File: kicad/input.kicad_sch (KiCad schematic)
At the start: 210 parts, among them J1 IN_1, J2 IN_2, Q1 CSD13380F3, Q5 CSD13380F3, SW1 RotaryEncoder, SW10 DG1411EEQ, SW11 DG1413EEQ, SW2 INST_IND_1, SW3 DG1413EEQ, SW4 DG1411EEQ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

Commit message: inst/line inverter
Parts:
- added C199, C200: 100nF, symbol Device:C
- added R127, R128, R129, R130: 1k, symbol Device:R_US
- added U24: OPA1612AxD, symbol Amplifier_Operational:OPA1612AxD
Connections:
- net +15V: now also C199.1, U24.8 (V+)
- net -15V: now also C200.1, U24.4 (V-)
- net GNDA: now also C199.2, C200.2, U24.3 (+), U24.6 (-); no longer SW11.3 (S1), SW5.3 (S1)
- net at R21.2, SW4.7 (D4), U5.1: now also SW5.3 (S1), R128.1; no longer SW5.6 (S4)
- net at R52.2, SW10.7 (D4): now also SW11.3 (S1), R129.1, U24.1; no longer SW11.6 (S4), U5.7
- net at R50.1, R57.2: now also U24.2 (-); no longer U5.5 (+)
- new net: R127.1, R128.2, U5.5 (+)
- new net: R127.2, SW5.6 (S4), U5.7
- new net: R130.2, SW11.6 (S4), U24.7
- new net: R129.2, R130.1, U24.5 (+)
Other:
- moved on the sheet: C187, C188, C70, Q1, R125, R126, R43, R45, R47, R48, R50, R51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

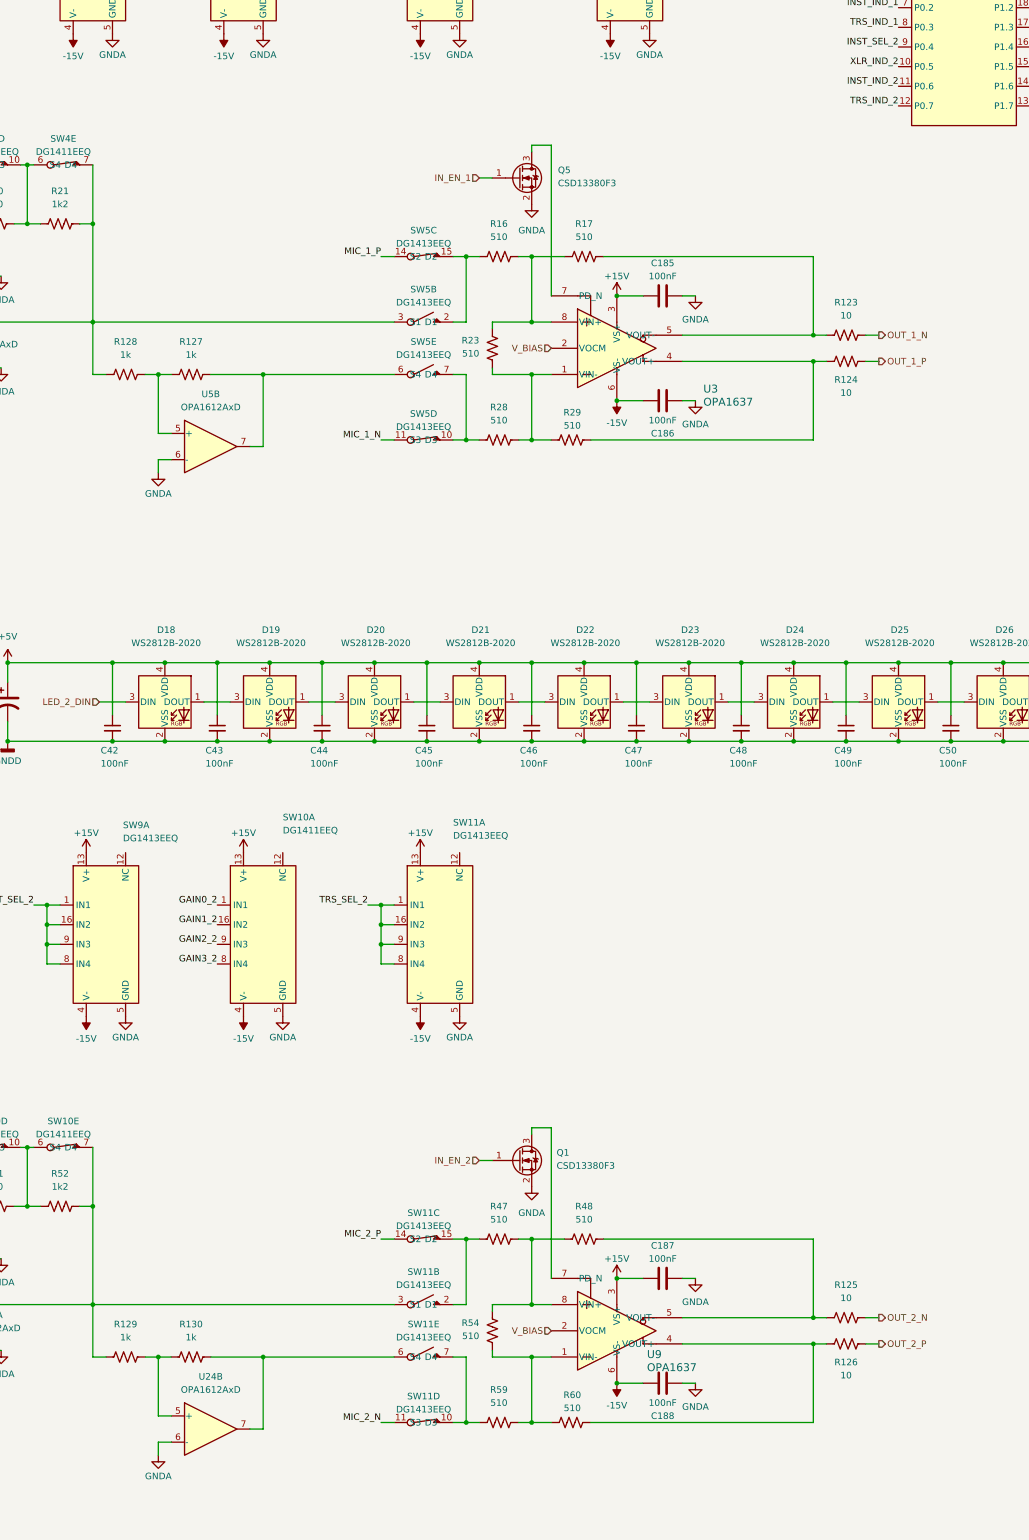
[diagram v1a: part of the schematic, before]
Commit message: OPA1637 impedance/inverter phase correction
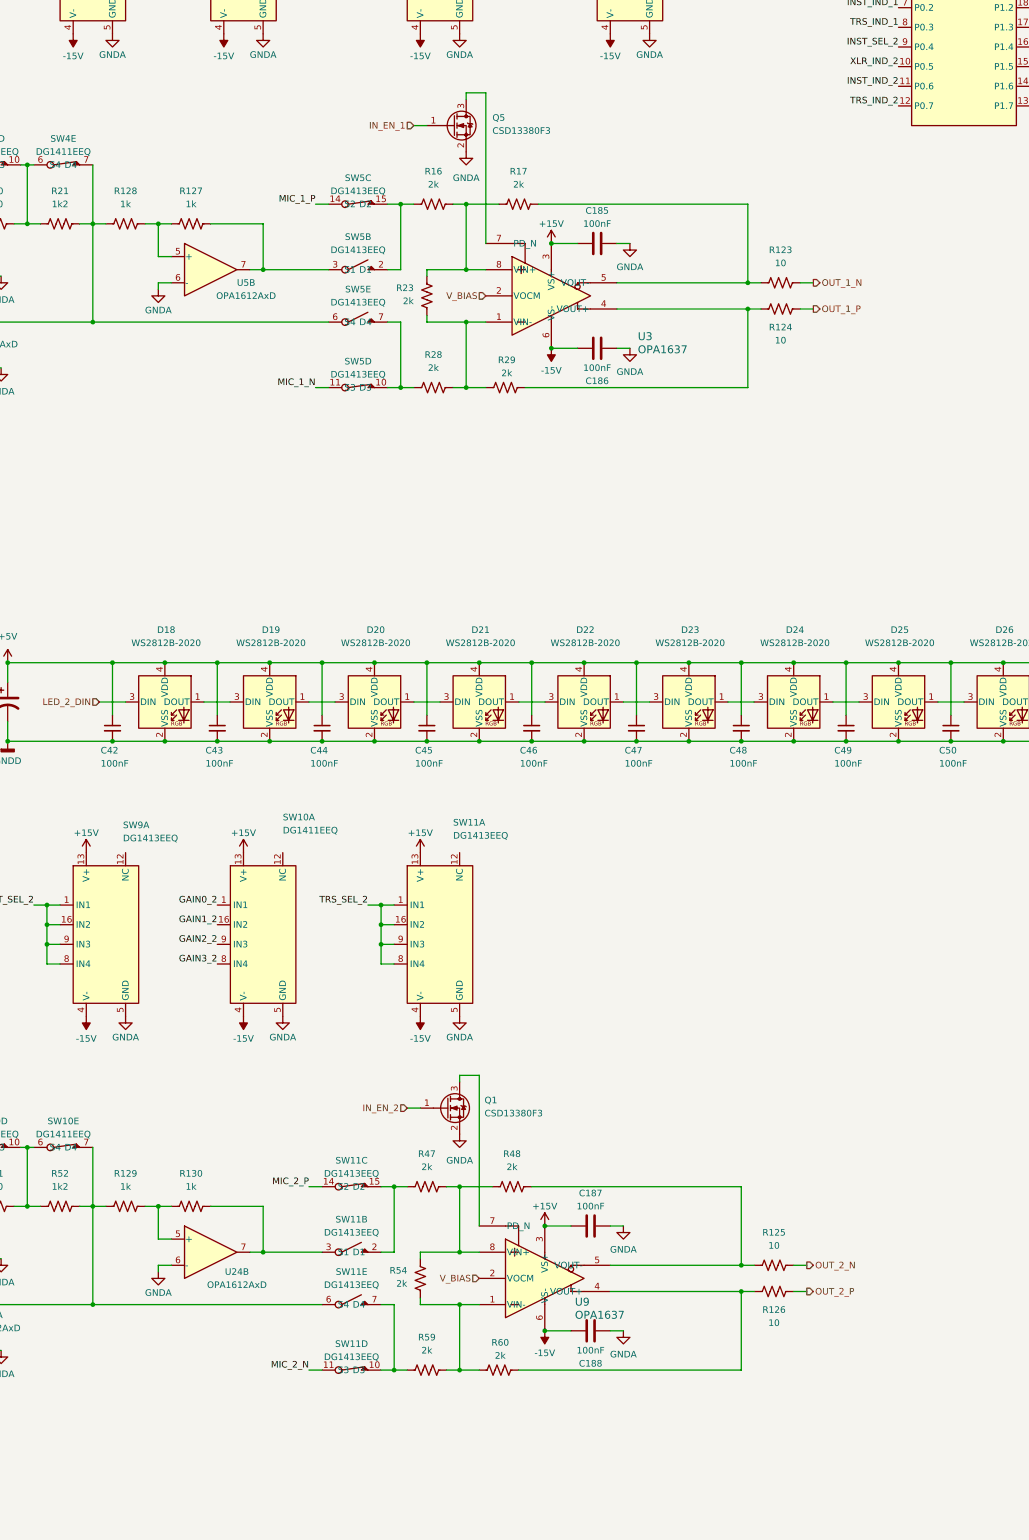
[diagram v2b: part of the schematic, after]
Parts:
- R16, R17, R23, R28, R29, R47, R48, R54, R59, R60: value 510 -> 2k
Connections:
- net at R129.1, R52.2, SW10.7 (D4)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: now also SW11.6 (S4); no longer SW11.3 (S1)
- net at R127.2, U5.7: now also SW5.3 (S1); no longer SW5.6 (S4)
- net at R130.2, U24.7: now also SW11.3 (S1); no longer SW11.6 (S4)
- net at R128.1, R21.2, SW4.7 (D4)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: now also SW5.6 (S4); no longer SW5.3 (S1)
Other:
- moved on the sheet: C185, C186, C187, C188, Q1, Q5, R123, R124, R125, R126, R127, R128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

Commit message: ac coupled inputs
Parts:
- added C201, C202, C203, C204: 10uF, symbol Device:C
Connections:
- net OUT_1_N: now also C203.2; no longer R123.2
- net OUT_1_P: now also C204.2; no longer R124.2
- net OUT_2_N: now also C201.2; no longer R125.2
- net OUT_2_P: now also C202.2; no longer R126.2
- new net: C204.1, R124.2
- new net: C201.1, R125.2
- new net: C203.1, R123.2
- new net: C202.1, R126.2

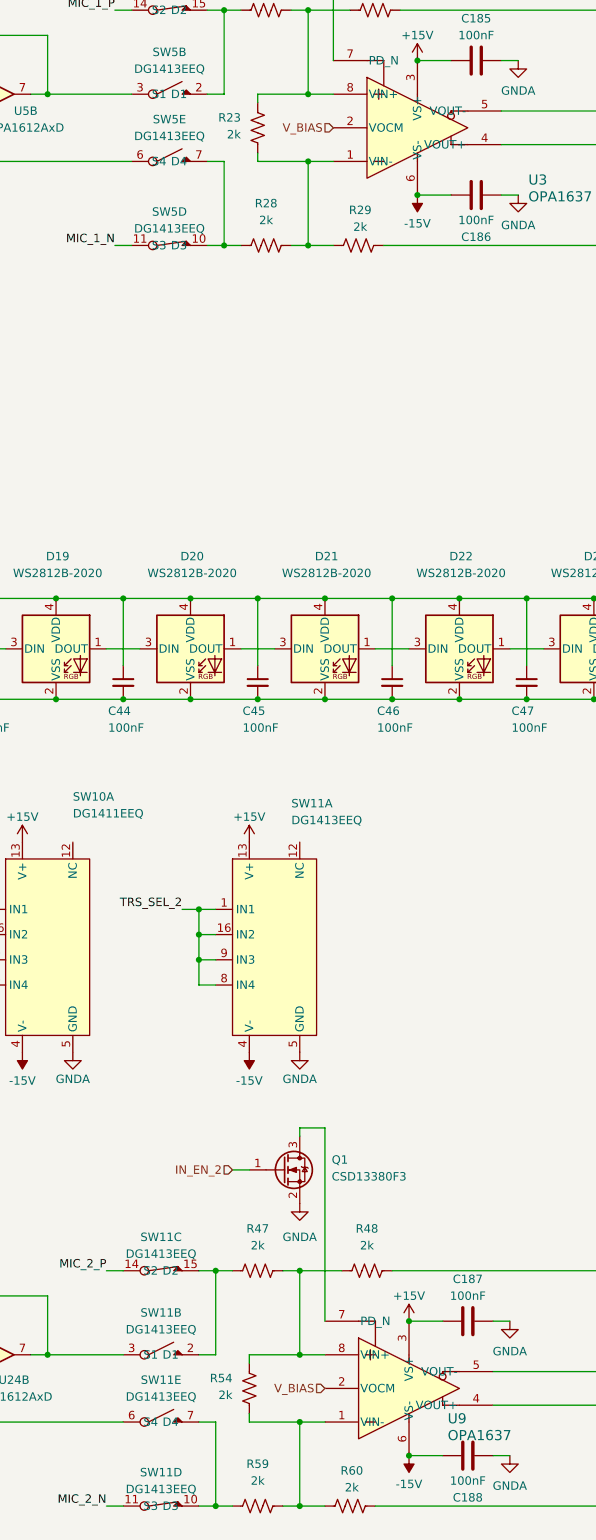
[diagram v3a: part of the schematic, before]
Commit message: remove mic vbias from inputs
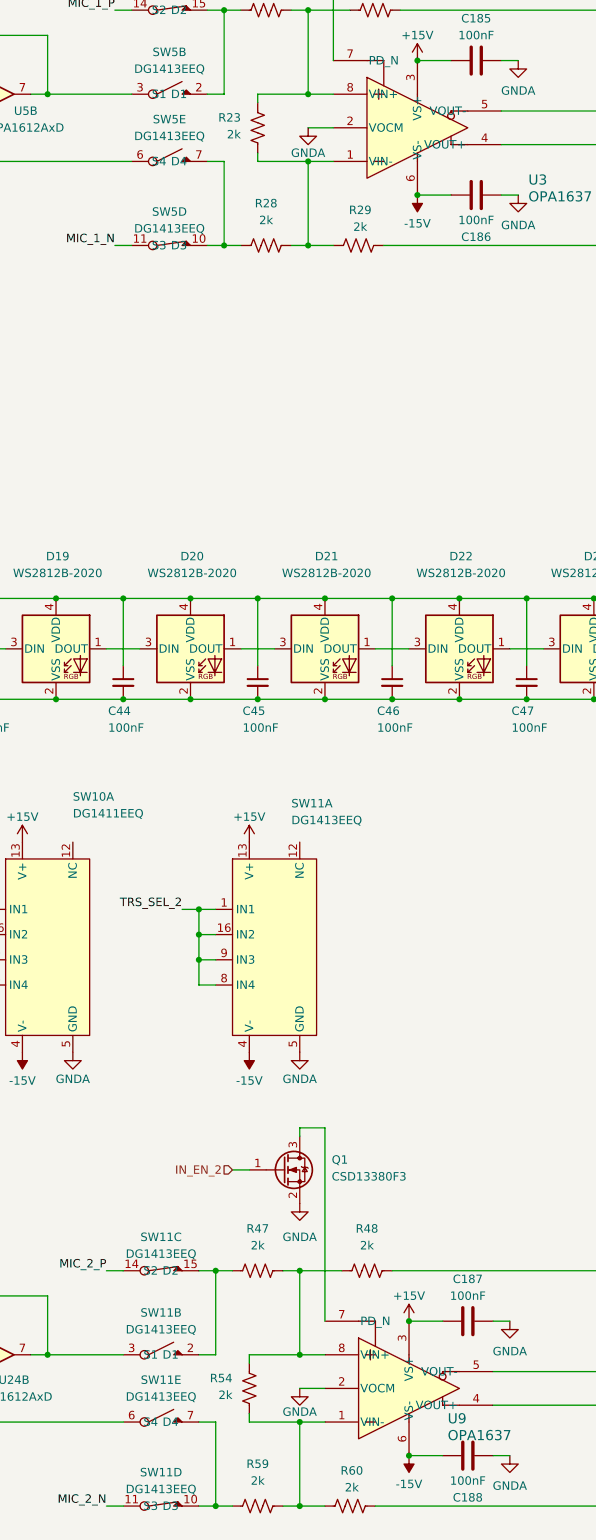
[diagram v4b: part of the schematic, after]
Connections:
- net V_BIAS is gone; now on net GNDA: U3.2 (VOCM), U9.2 (VOCM)
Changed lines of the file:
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@@
 	(wire
 		(pts
+			(xy 350.52 350.52) (xy 354.33 350.52)
+		)
+		(stroke
+			(width 0)
+			(type default)
+		)
+	)
+	(wire
+		(pts
 			(xy 283.21 246.38) (xy 293.37 246.38)
 		)
@@
 	(wire
 		(pts
+			(xy 351.79 160.02) (xy 355.6 160.02)
+		)
+		(stroke
+			(width 0)
+			(type default)
+		)
+	)
+	(wire
+		(pts
 			(xy 382.27 36.83) (xy 387.35 36.83)
 		)
@@
 		)
 	)
-	(hierarchical_label "V_BIAS"
-		(shape input)
-		(at 355.6 160.02 180)
-		(effects
-			(font
-				(size 1.27 1.27)
-			)
-			(justify right)
-		)
-	)
 	(hierarchical_label "DOUT"
 		(shape output)
@@
 		)
 	)
-	(hierarchical_label "V_BIAS"
-		(shape input)
-		(at 354.33 350.52 180)
-		(effects
-			(font
-				(size 1.27 1.27)
-			)
-			(justify right)
-		)
-	)
 	(symbol
 		(lib_id "power:+15V")
@@
 	)
 	(symbol
+		(lib_id "power:GNDA")
+		(at 350.52 350.52 0)
+		(unit 1)
+		(body_style 1)
+		(exclude_from_sim no)
+		(in_bom yes)
+		(on_board yes)
+		(in_pos_files yes)
+		(dnp no)
+		(property "Reference" "#PWR0250"
+			(at 350.52 356.87 0)
+			(hide yes)
+			(show_name no)
+			(do_not_autoplace no)
+			(effects
+				(font
+					(size 1.27 1.27)
+				)
+			)
+		)
+		(property "Value" "GNDA"
+			(at 350.52 354.076 0)
+			(show_name no)
+			(do_not_autoplace no)
+			(effects
+				(font
+					(size 1.27 1.27)
+				)
+			)
+		)
+		(property "Footprint" ""
+			(at 350.52 350.52 0)
+			(hide yes)
+			(show_name no)
+			(do_not_autoplace no)
+			(effects
+				(font
+					(size 1.27 1.27)
+				)
+			)
+		)
+		(property "Datasheet" ""
+			(at 350.52 350.52 0)
+			(hide yes)
+			(show_name no)
+			(do_not_autoplace no)
+			(effects
+				(font
+					(size 1.27 1.27)
+				)
+			)
+		)
+		(property "Description" "Power symbol creates a global label with name \"GNDA\" , analog ground"
+			(at 350.52 350.52 0)
+			(hide yes)
+			(show_name no)
+			(do_not_autoplace no)
+			(effects
+				(font
+					(size 1.27 1.27)
+				)
+			)
+		)
+		(pin "1"
+		)
+		(instances
+			(project "openmic"
+				(path "/84faeadc-8b12-4a66-a17f-5c56e5923fb8/305fc275-c4c3-417f-b998-113f7e74be2d"
+					(reference "#PWR0250")
+					(unit 1)
+				)
+			)
+		)
+	)
+	(symbol
 		(lib_id "LED:WS2812B-2020")
 		(at 496.57 36.83 0)
@@
 					(unit 1)
 				)
+			)
+		)
+	)
+	(symbol
+		(lib_id "power:GNDA")
+		(at 351.79 160.02 0)
+		(unit 1)
+		(body_style 1)
+		(exclude_from_sim no)
+		(in_bom yes)
+		(on_board yes)
+		(in_pos_files yes)
+		(dnp no)
+		(property "Reference" "#PWR0251"
+			(at 351.79 166.37 0)
+			(hide yes)
+			(show_name no)
+			(do_not_autoplace no)
+			(effects
+				(font
+					(size 1.27 1.27)
+				)
+			)
+		)
+		(property "Value" "GNDA"
+			(at 351.79 163.83 0)
+			(show_name no)
+			(do_not_autoplace no)
+			(effects
+				(font
+					(size 1.27 1.27)
+				)
+			)
+		)
+		(property "Footprint" ""
+			(at 351.79 160.02 0)
+			(hide yes)
+			(show_name no)
+			(do_not_autoplace no)
+			(effects
+				(font
+					(size 1.27 1.27)
+				)
+			)
+		)
+		(property "Datasheet" ""
+			(at 351.79 160.02 0)
+			(hide yes)
+			(show_name no)
+			(do_not_autoplace no)
+			(effects
+				(font
+					(size 1.27 1.27)
+				)
+			)
+		)
+		(property "Description" "Power symbol creates a global label with name \"GNDA\" , analog ground"
+			(at 351.79 160.02 0)
+			(hide yes)
+			(show_name no)
+			(do_not_autoplace no)
+			(effects
+				(font
+					(size 1.27 1.27)
+				)
+			)
+		)
+		(pin "1"
+		)
+		(instances
+			(project "openmic"
+				(path "/84faeadc-8b12-4a66-a17f-5c56e5923fb8/305fc275-c4c3-417f-b998-113f7e74be2d"
+					(reference "#PWR0251")
+					(unit 1)
+				)

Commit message: #16
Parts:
- removed C27, C65: 100nF, symbol Device:C
- removed J1: IN_1, symbol Connector_Audio:XLR3_AudioJack3_Combo_GroundSwitch_Switch
- removed J2: IN_2, symbol Connector_Audio:XLR3_AudioJack3_Combo_GroundSwitch_Switch
- removed R12, R41: 47k, symbol Device:R_US
- added J1: IN_1, symbol Connector_Audio:XLR3_AudioJack3_Combo_Ground_Switch
- added J2: IN_2, symbol Connector_Audio:XLR3_AudioJack3_Combo_Ground_Switch
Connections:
- net XLR_IND_1 is gone; now on net TRS_SEL_1: U8.6 (P0.1)
- net XLR_IND_2 is gone; now on net TRS_SEL_2: U8.10 (P0.5)
- net GNDA: now also J1.1, J1.G, J1.RN, J1.S, J1.TN, J2.1, J2.G, J2.RN, J2.S, J2.TN
- net IN_EN_1: now also U1.19 (GPO_CH1)
- net IN_EN_2: now also U1.20 (GPO_CH2)
- net TRS_SEL_1: no longer U1.19 (GPO_CH1)
- net TRS_SEL_2: no longer U1.20 (GPO_CH2)
- net at C75.1, SW9.11 (S3), SW9.6 (S4): now also J2.T
- net at C60.1, C61.1, C63.1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: now also J2.2
- net at C63.2, C66.1, C67.1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: now also J2.3
- net at C36.1, SW3.11 (S3), SW3.6 (S4): now also J1.T
- net at C76.1, SW9.14 (S2), SW9.3 (S1): now also J2.R
- net at C72.1: now also J2.SN
- net at C25.2, C28.1, C29.1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: now also J1.3
- net at C37.1, SW3.14 (S2), SW3.3 (S1): now also J1.R
- net at C33.1: now also J1.SN
- net at C22.1, C23.1, C25.1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: now also J1.2
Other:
- moved on the sheet: C36, C37, C75, C76

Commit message: added protection diodes
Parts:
- removed D14, D15, D16, D17, D31, D32, D33, D34: D, symbol Device:D
- removed R58: 100, symbol Device:R_US
- added D14, D15, D16, D17, D65, D66, D67, D68: BAV99, Package_TO_SOT_SMD:SOT-23, symbol Diode:BAV99
- added R41: 100, symbol Device:R_US
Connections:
- net +15V: now also D14.2 (A), D15.2 (A), D16.2 (A), D17.2 (A), D65.2 (A), D66.2 (A), D67.2 (A), D68.2 (A)
- net -15V: now also D14.1 (K), D15.1 (K), D16.1 (K), D17.1 (K), D65.1 (K), D66.1 (K), D67.1 (K), D68.1 (K)
- net at C24.1, C26.1, R10.2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: now also D14.3 (K)
- net at C74.1, R53.2, U10.2 (IN-): now also D68.3 (K)
- net at C77.2, U10.3 (IN+): now also SW9.10 (D3)
- net at C62.1, C64.1, R39.2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: now also D16.3 (K)
- net at C35.1, R22.2, U4.2 (IN-): now also D66.3 (K)
- net at C75.1, J2.T: now also R41.1; no longer SW9.11 (S3), SW9.6 (S4)
- net at C26.2, C30.1, R13.2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: now also D15.3 (K)
- net at SW3.10 (D3): now also C38.2, U4.3 (IN+); no longer R27.1
- net at SW3.11 (S3), SW3.6 (S4): now also R27.2, D65.3 (K); no longer C36.1, J1.T
- net at C64.2, C68.1, R42.2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: now also D17.3 (K)
- new net: D67.3 (K), R41.2, SW9.11 (S3), SW9.6 (S4)
- new net: C36.1, J1.T, R27.1
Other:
- note added: "design note: The OPA1637's output current is limited to +/-31mA, so the clamping diodes at the TAC5212 inputs will never see more than this. This means the series resistor value doesn't matter and only servers to isolate the circuit, not limit the current through the schottky diodes."
- moved on the sheet: C181, C182, C183, C184, C185, C186, C187, C188, C199, C200, C201, C202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
